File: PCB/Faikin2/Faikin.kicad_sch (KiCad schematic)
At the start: 30 parts, among them J1 1x5, J2 Prog, Q1 BSS138PS, U1 ESP32-PICO-MINI-02, U2 Barcode, U3 MD8942

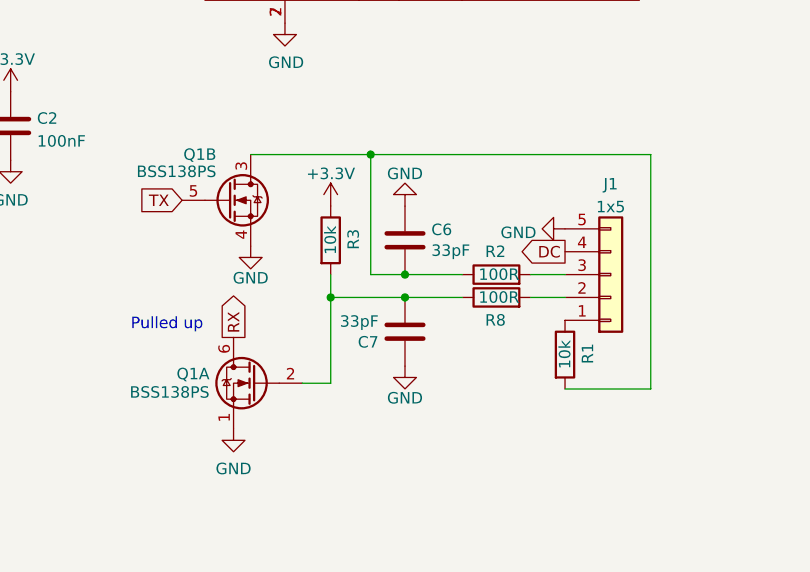
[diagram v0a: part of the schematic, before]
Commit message: New single sided board design
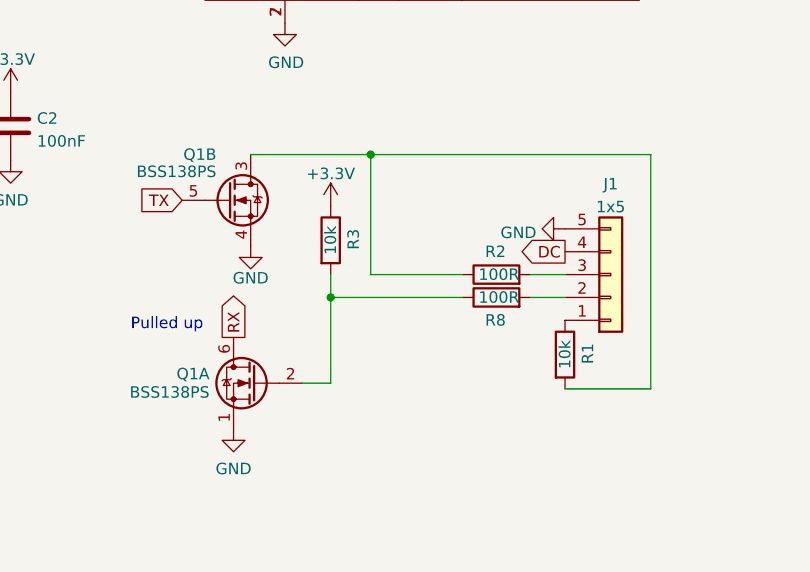
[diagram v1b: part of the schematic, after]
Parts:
- removed C6, C7: 33pF, RevK:C_0402, symbol Device:C
- Q1: LCSC Part # C193381 -> C2912548
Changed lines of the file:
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@@
     (comment 2 "www.me.uk")
   )
-  (junction (at 143.51 88.9) (diameter 0) (color 0 0 0 0)
-  )
   (junction (at 50.8 43.18) (diameter 0) (color 0 0 0 0)
   )
   (junction (at 50.8 27.94) (diameter 0) (color 0 0 0 0)
-  )
-  (junction (at 143.51 91.44) (diameter 0) (color 0 0 0 0)
   )
   (junction (at 81.28 52.07) (diameter 0) (color 0 0 0 0)
@@
     (stroke (width 0) (type default))
   )
-  (wire (pts (xy 143.51 91.44) (xy 149.86 91.44))
+  (wire (pts (xy 135.255 91.44) (xy 149.86 91.44))
     (stroke (width 0) (type default))
   )
@@
     (stroke (width 0) (type default))
   )
-  (wire (pts (xy 139.7 88.9) (xy 143.51 88.9))
-    (stroke (width 0) (type default))
-  )
   (wire (pts (xy 170.815 75.565) (xy 170.815 101.6))
     (stroke (width 0) (type default))
@@
     (stroke (width 0) (type default))
   )
-  (wire (pts (xy 135.255 91.44) (xy 143.51 91.44))
-    (stroke (width 0) (type default))
-  )
   (wire (pts (xy 81.28 52.07) (xy 86.36 52.07))
     (stroke (width 0) (type default))
@@
     (stroke (width 0) (type default))
   )
-  (wire (pts (xy 143.51 88.9) (xy 149.86 88.9))
+  (wire (pts (xy 139.7 88.9) (xy 149.86 88.9))
     (stroke (width 0) (type default))
   )
@@
     )
   )
-  (symbol (lib_id "Device:C") (at 143.51 95.25 180) (unit 1)
-    (in_bom yes) (on_board yes) (dnp no)
-    (property "Reference" "C7" (at 140.589 96.4184 0)
-      (effects (font (size 1.27 1.27)) (justify left))
-    )
-    (property "Value" "33pF" (at 140.589 94.107 0)
-      (effects (font (size 1.27 1.27)) (justify left))
-    )
-    (property "Footprint" "RevK:C_0402" (at 142.5448 91.44 0)
-      (effects (font (size 1.27 1.27)) hide)
-    )
-    (property "Datasheet" "" (at 143.51 95.25 0)
-      (effects (font (size 1.27 1.27)) hide)
-    )
-    (property "Note" "" (at 143.51 95.25 0)
-      (effects (font (size 1.27 1.27)) hide)
-    )
-    (property "Manufacturer" "" (at 143.51 95.25 0)
-      (effects (font (size 1.27 1.27)) hide)
-    )
-    (pin "1")
-    (pin "2")
-    (instances
-      (project "Faikin"
-        (path "/46c350bb-7de4-4e81-aafd-4af55e37aab0"
-          (reference "C7") (unit 1)
-        )
-      )
-    )
-  )
   (symbol (lib_id "Device:C") (at 99.695 72.39 0) (unit 1)
     (in_bom yes) (on_board yes) (dnp no) (fields_autoplaced)
@@
       (effects (font (size 1.27 1.27)) hide)
     )
-    (property "LCSC Part #" "C193381" (at 133.35 74.676 0)
+    (property "LCSC Part #" "C2912548" (at 133.35 74.676 0)
       (effects (font (size 1.27 1.27)) hide)
     )
@@
     )
   )
-  (symbol (lib_id "Device:C") (at 143.51 85.09 0) (unit 1)
-    (in_bom yes) (on_board yes) (dnp no)
-    (property "Reference" "C6" (at 146.431 83.9216 0)
-      (effects (font (size 1.27 1.27)) (justify left))
-    )
-    (property "Value" "33pF" (at 146.431 86.233 0)
-      (effects (font (size 1.27 1.27)) (justify left))
-    )
-    (property "Footprint" "RevK:C_0402" (at 144.4752 88.9 0)
-      (effects (font (size 1.27 1.27)) hide)
-    )
-    (property "Datasheet" "" (at 143.51 85.09 0)
-      (effects (font (size 1.27 1.27)) hide)
-    )
-    (property "Note" "" (at 143.51 85.09 0)
-      (effects (font (size 1.27 1.27)) hide)
-    )
-    (property "Manufacturer" "" (at 143.51 85.09 0)
-      (effects (font (size 1.27 1.27)) hide)
-    )
-    (pin "1")
-    (pin "2")
-    (instances
-      (project "Faikin"
-        (path "/46c350bb-7de4-4e81-aafd-4af55e37aab0"
-          (reference "C6") (unit 1)
-        )
-      )
-    )
-  )
   (symbol (lib_id "Device:R") (at 153.67 88.9 90) (unit 1)
     (in_bom yes) (on_board yes) (dnp no)
@@
         (path "/babeabf2-f3b0-4ed5-8d9e-0215947e6cf3"
           (reference "R8") (unit 1)
-        )
-      )
-    )
-  )
-  (symbol (lib_id "power:GND") (at 143.51 99.06 0) (unit 1)
-    (in_bom yes) (on_board yes) (dnp no) (fields_autoplaced)
-    (property "Reference" "#PWR0112" (at 143.51 105.41 0)
-      (effects (font (size 1.27 1.27)) hide)
-    )
-    (property "Value" "GND" (at 143.51 102.6358 0)
-      (effects (font (size 1.27 1.27)))
-    )
-    (property "Footprint" "" (at 143.51 99.06 0)
-      (effects (font (size 1.27 1.27)) hide)
-    )
-    (property "Datasheet" "" (at 143.51 99.06 0)
-      (effects (font (size 1.27 1.27)) hide)
-    )
-    (pin "1")
-    (instances
-      (project "Faikin"
-        (path "/46c350bb-7de4-4e81-aafd-4af55e37aab0"
-          (reference "#PWR0112") (unit 1)
         )
       )
@@
       (effects (font (size 1.27 1.27)) hide)
     )
-    (property "LCSC Part #" "C193381" (at 117.475 94.996 0)
+    (property "LCSC Part #" "C2912548" (at 117.475 94.996 0)
       (effects (font (size 1.27 1.27)) hide)
     )
@@
         )
       )
-    )
-  )
-  (symbol (lib_id "power:GND") (at 143.51 81.28 180) (unit 1)
-    (in_bom yes) (on_board yes) (dnp no) (fields_autoplaced)
-    (property "Reference" "#PWR0111" (at 143.51 74.93 0)
-      (effects (font (size 1.27 1.27)) hide)
-    )
-    (property "Value" "GND" (at 143.51 77.7042 0)
-      (effects (font (size 1.27 1.27)))
-    )
-    (property "Footprint" "" (at 143.51 81.28 0)
-      (effects (font (size 1.27 1.27)) hide)
-    )
-    (property "Datasheet" "" (at 143.51 81.28 0)
-      (effects (font (size 1.27 1.27)) hide)
-    )
-    (pin "1")
-    (instances
-      (project "Faikin"
-        (path "/46c350bb-7de4-4e81-aafd-4af55e37aab0"
-          (reference "#PWR0111") (unit 1)
-        )
-      )

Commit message: As ordered
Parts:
- added C3, C4: 33pF, RevK:C_0402, symbol Device:C
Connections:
- net GND: now also C3.1, C4.1
- net at Q1.2 (GN), R3.2, R8.1: now also C4.2
- net at Q1.3 (SP), R1.2, R2.1: now also C3.2
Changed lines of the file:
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@@
   (junction (at 81.28 57.15) (diameter 0) (color 0 0 0 0)
+  )
+  (junction (at 143.51 91.44) (diameter 0) (color 0 0 0 0)
+  )
+  (junction (at 143.51 88.9) (diameter 0) (color 0 0 0 0)
   )
   (no_connect (at 81.28 71.12))
@@
     (stroke (width 0) (type default))
   )
-  (wire (pts (xy 135.255 91.44) (xy 149.86 91.44))
+  (wire (pts (xy 135.255 91.44) (xy 143.51 91.44))
     (stroke (width 0) (type default))
   )
@@
     (stroke (width 0) (type default))
   )
+  (wire (pts (xy 143.51 88.9) (xy 149.86 88.9))
+    (stroke (width 0) (type default))
+  )
   (wire (pts (xy 170.815 75.565) (xy 170.815 101.6))
     (stroke (width 0) (type default))
@@
     (stroke (width 0) (type default))
   )
-  (wire (pts (xy 139.7 88.9) (xy 149.86 88.9))
+  (wire (pts (xy 139.7 88.9) (xy 143.51 88.9))
     (stroke (width 0) (type default))
   )
   (wire (pts (xy 139.7 75.565) (xy 139.7 88.9))
+    (stroke (width 0) (type default))
+  )
+  (wire (pts (xy 143.51 91.44) (xy 149.86 91.44))
     (stroke (width 0) (type default))
   )
@@
     )
   )
+  (symbol (lib_id "power:GND") (at 143.51 99.06 0) (unit 1)
+    (in_bom yes) (on_board yes) (dnp no) (fields_autoplaced)
+    (property "Reference" "#PWR010" (at 143.51 105.41 0)
+      (effects (font (size 1.27 1.27)) hide)
+    )
+    (property "Value" "GND" (at 143.51 102.6358 0)
+      (effects (font (size 1.27 1.27)))
+    )
+    (property "Footprint" "" (at 143.51 99.06 0)
+      (effects (font (size 1.27 1.27)) hide)
+    )
+    (property "Datasheet" "" (at 143.51 99.06 0)
+      (effects (font (size 1.27 1.27)) hide)
+    )
+    (pin "1")
+    (instances
+      (project "Faikin"
+        (path "/46c350bb-7de4-4e81-aafd-4af55e37aab0"
+          (reference "#PWR010") (unit 1)
+        )
+      )
+    )
+  )
   (symbol (lib_id "Device:R") (at 64.77 27.94 270) (unit 1)
     (in_bom yes) (on_board yes) (dnp no)
@@
         (path "/46c350bb-7de4-4e81-aafd-4af55e37aab0"
           (reference "PCB1") (unit 1)
+        )
+      )
+    )
+  )
+  (symbol (lib_id "power:GND") (at 143.51 81.28 180) (unit 1)
+    (in_bom yes) (on_board yes) (dnp no) (fields_autoplaced)
+    (property "Reference" "#PWR07" (at 143.51 74.93 0)
+      (effects (font (size 1.27 1.27)) hide)
+    )
+    (property "Value" "GND" (at 143.51 77.7042 0)
+      (effects (font (size 1.27 1.27)))
+    )
+    (property "Footprint" "" (at 143.51 81.28 0)
+      (effects (font (size 1.27 1.27)) hide)
+    )
+    (property "Datasheet" "" (at 143.51 81.28 0)
+      (effects (font (size 1.27 1.27)) hide)
+    )
+    (pin "1")
+    (instances
+      (project "Faikin"
+        (path "/46c350bb-7de4-4e81-aafd-4af55e37aab0"
+          (reference "#PWR07") (unit 1)
         )
       )
@@
     )
   )
+  (symbol (lib_id "Device:C") (at 143.51 95.25 180) (unit 1)
+    (in_bom yes) (on_board yes) (dnp no)
+    (property "Reference" "C4" (at 140.589 96.4184 0)
+      (effects (font (size 1.27 1.27)) (justify left))
+    )
+    (property "Value" "33pF" (at 140.589 94.107 0)
+      (effects (font (size 1.27 1.27)) (justify left))
+    )
+    (property "Footprint" "RevK:C_0402" (at 142.5448 91.44 0)
+      (effects (font (size 1.27 1.27)) hide)
+    )
+    (property "Datasheet" "" (at 143.51 95.25 0)
+      (effects (font (size 1.27 1.27)) hide)
+    )
+    (property "Note" "" (at 143.51 95.25 0)
+      (effects (font (size 1.27 1.27)) hide)
+    )
+    (property "Manufacturer" "" (at 143.51 95.25 0)
+      (effects (font (size 1.27 1.27)) hide)
+    )
+    (pin "1")
+    (pin "2")
+    (instances
+      (project "Faikin"
+        (path "/46c350bb-7de4-4e81-aafd-4af55e37aab0"
+          (reference "C4") (unit 1)
+        )
+      )
+    )
+  )
   (symbol (lib_id "RevK:Hidden") (at 151.13 46.99 0) (unit 1)
     (in_bom yes) (on_board yes) (dnp no)
@@
         )
       )
+    )
+  )
+  (symbol (lib_id "Device:C") (at 143.51 85.09 0) (unit 1)
+    (in_bom yes) (on_board yes) (dnp no)
+    (property "Reference" "C3" (at 146.431 83.9216 0)
+      (effects (font (size 1.27 1.27)) (justify left))
+    )
+    (property "Value" "33pF" (at 146.431 86.233 0)
+      (effects (font (size 1.27 1.27)) (justify left))
+    )
+    (property "Footprint" "RevK:C_0402" (at 144.4752 88.9 0)
+      (effects (font (size 1.27 1.27)) hide)
+    )
+    (property "Datasheet" "" (at 143.51 85.09 0)
+      (effects (font (size 1.27 1.27)) hide)
+    )
+    (property "Note" "" (at 143.51 85.09 0)
+      (effects (font (size 1.27 1.27)) hide)
+    )
+    (property "Manufacturer" "" (at 143.51 85.09 0)
+      (effects (font (size 1.27 1.27)) hide)
+    )
+    (pin "1")
+    (pin "2")
+    (instances
+      (project "Faikin"
+        (path "/46c350bb-7de4-4e81-aafd-4af55e37aab0"
+          (reference "C3") (unit 1)
+        )
+      )

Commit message: Silk
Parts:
- added Logo1: AJK, RevK:AJK, symbol RevK:AJK
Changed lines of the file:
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@@
+    )
+  )
+  (symbol (lib_id "RevK:AJK") (at 250.19 174.625 0) (unit 1)
+    (in_bom no) (on_board yes) (dnp no) (fields_autoplaced)
+    (property "Reference" "Logo1" (at 250.19 172.085 0)
+      (effects (font (size 1.27 1.27)) hide)
+    )
+    (property "Value" "AJK" (at 250.825 174.625 0)
+      (effects (font (size 1.27 1.27)) (justify left))
+    )
+    (property "Footprint" "RevK:AJK" (at 250.19 177.165 0)
+      (effects (font (size 1.27 1.27)) hide)
+    )
+    (property "Datasheet" "" (at 250.19 177.165 0)
+      (effects (font (size 1.27 1.27)) hide)
+    )
+    (property "Note" "Non part, PCB printed" (at 250.19 174.625 0)
+      (effects (font (size 1.27 1.27)) hide)
+    )
+    (instances
+      (project "Faikin"
+        (path "/46c350bb-7de4-4e81-aafd-4af55e37aab0"
+          (reference "Logo1") (unit 1)
+        )
+      )
     )
   )

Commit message: Library update
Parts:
- removed R3: 10k, RevK:R_0402, symbol Device:R
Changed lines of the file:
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@@
   (junction (at 81.28 52.07) (diameter 0) (color 0 0 0 0)
-  )
-  (junction (at 135.255 91.44) (diameter 0) (color 0 0 0 0)
   )
   (junction (at 139.7 75.565) (diameter 0) (color 0 0 0 0)
@@
     (stroke (width 0) (type default))
   )
-  (wire (pts (xy 135.255 88.9) (xy 135.255 91.44))
-    (stroke (width 0) (type default))
-  )
   (wire (pts (xy 81.28 52.07) (xy 86.36 52.07))
     (stroke (width 0) (type default))
@@
         )
       )
-    )
-  )
-  (symbol (lib_id "Device:R") (at 135.255 85.09 0) (unit 1)
-    (in_bom yes) (on_board yes) (dnp no)
-    (property "Reference" "R3" (at 137.795 83.82 90)
-      (effects (font (size 1.27 1.27)) (justify right))
-    )
-    (property "Value" "10k" (at 135.255 85.09 90)
-      (effects (font (size 1.27 1.27)))
-    )
-    (property "Footprint" "RevK:R_0402" (at 133.477 85.09 90)
-      (effects (font (size 1.27 1.27)) hide)
-    )
-    (property "Datasheet" "~" (at 135.255 85.09 0)
-      (effects (font (size 1.27 1.27)) hide)
-    )
-    (pin "1")
-    (pin "2")
-    (instances
-      (project "Faikin"
-        (path "/46c350bb-7de4-4e81-aafd-4af55e37aab0"
-          (reference "R3") (unit 1)
-        )
-      )
-    )
-  )
-  (symbol (lib_id "power:+3.3V") (at 135.255 81.28 0) (unit 1)
-    (in_bom yes) (on_board yes) (dnp no) (fields_autoplaced)
-    (property "Reference" "#PWR06" (at 135.255 85.09 0)
-      (effects (font (size 1.27 1.27)) hide)
-    )
-    (property "Value" "+3.3V" (at 135.255 77.7042 0)
-      (effects (font (size 1.27 1.27)))
-    )
-    (property "Footprint" "" (at 135.255 81.28 0)
-      (effects (font (size 1.27 1.27)) hide)
-    )
-    (property "Datasheet" "" (at 135.255 81.28 0)
-      (effects (font (size 1.27 1.27)) hide)
-    )
-    (pin "1")
-    (instances
-      (project "Faikin"
-        (path "/46c350bb-7de4-4e81-aafd-4af55e37aab0"
-          (reference "#PWR06") (unit 1)
-        )
-      )

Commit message: Mainly #83
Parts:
- J1: LCSC Part # C225427 -> C265103
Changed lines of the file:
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@@
       (effects (font (size 1.27 1.27)) hide)
     )
-    (property "LCSC Part #" "C225427" (at 166.37 88.9 0)
+    (property "LCSC Part #" "C265103" (at 166.37 88.9 0)
       (effects (font (size 1.27 1.27)) hide)
     )

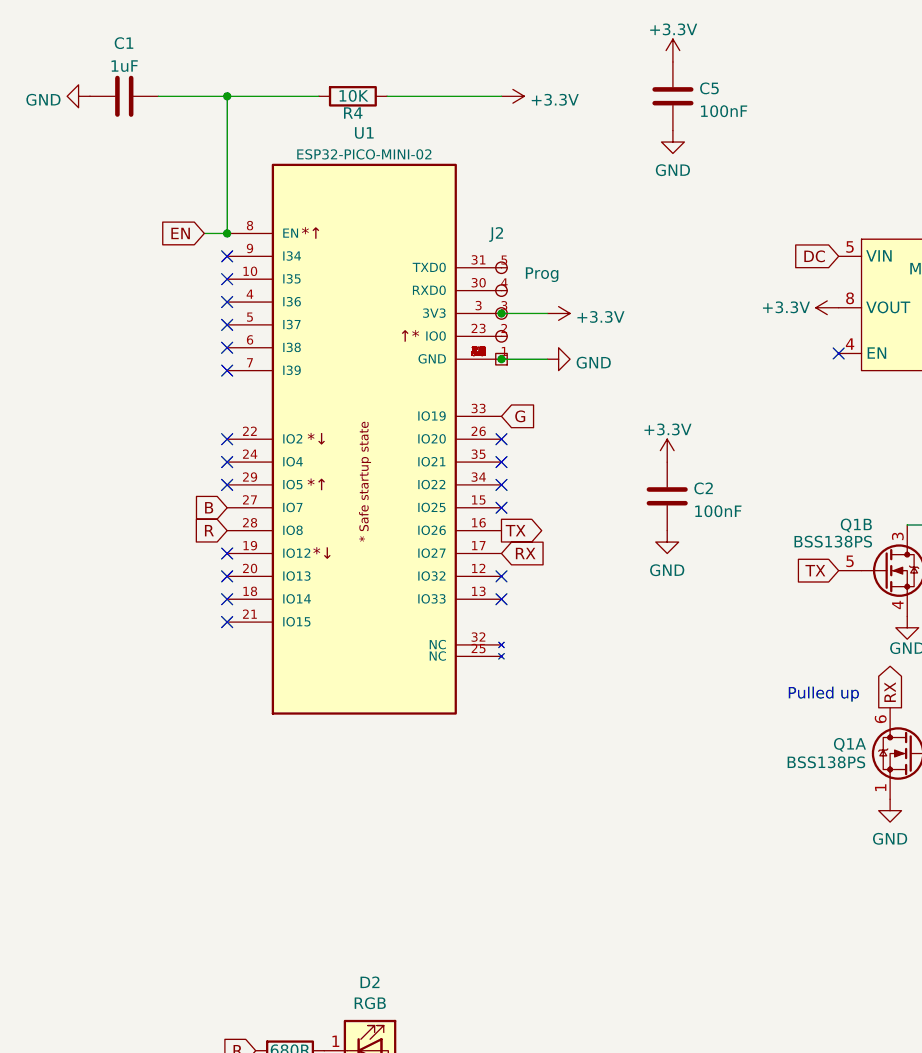
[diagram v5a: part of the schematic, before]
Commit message: Faikin2 confirmed working, now replaces Faikin 1
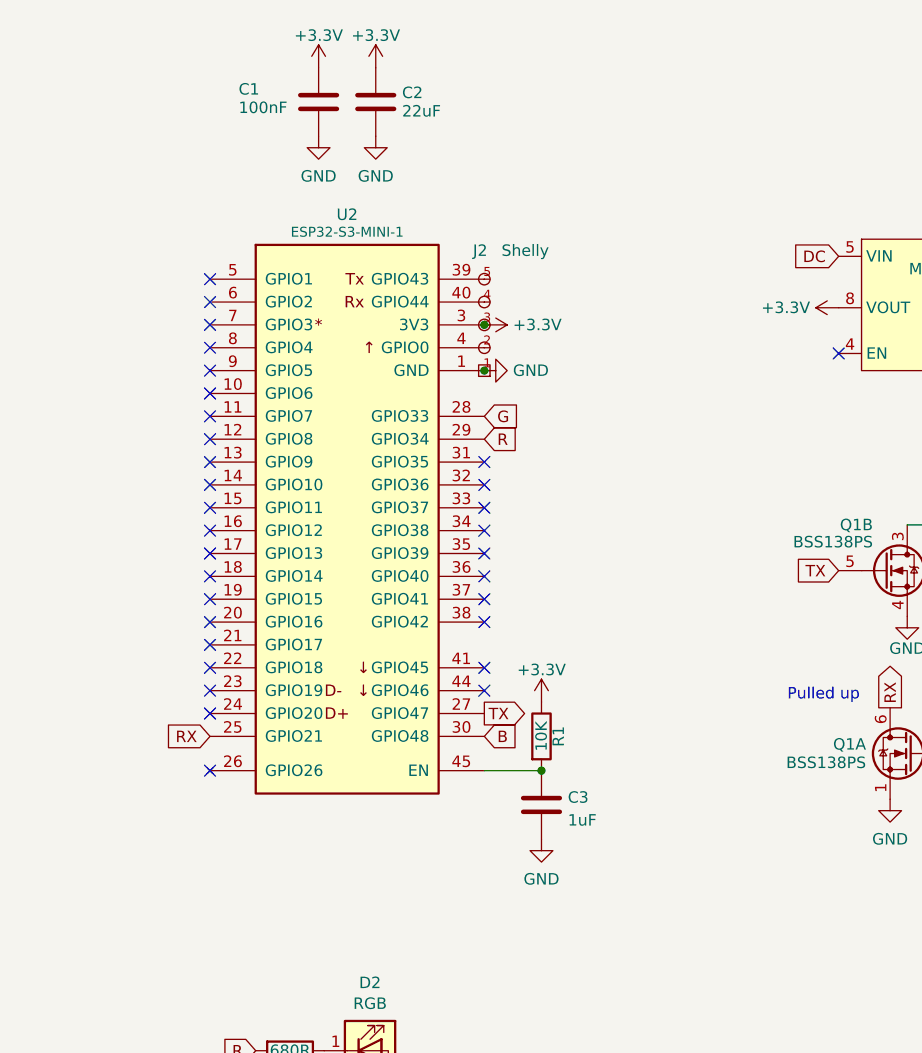
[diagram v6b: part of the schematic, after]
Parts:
- removed C5: 100nF, RevK:C_0402, symbol Device:C
- removed R4: 10K, RevK:R_0402, symbol Device:R
- removed U1: ESP32-PICO-MINI-02, RevK:ESP32-PICO-MINI-02, symbol RevK:ESP32-PICO-MINI-02
- added C3: 1uF, RevK:C_0402, symbol Device:C
- added R1: 10K, RevK:R_0402, symbol Device:R
- added U2: ESP32-S3-MINI-1, RevK:ESP32-S3-MINI-1, symbol RevK:ESP32-S3-MINI-1-N4R2
- C1: value 1uF -> 100nF
- C2: value 100nF -> 22uF
- J2: value Prog -> Shelly
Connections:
- net EN is gone; now on net GND: C1.2
- net +3.3V: now also C1.1, R1.1, U2.3 (3V3)
- net B: now also U2.30 (GPIO48)
- net G: now also U2.28 (GPIO33)
- net GND: now also C3.2, U2.1 (GND), U2.2 (GND), U2.42 (GND), U2.43 (GND), U2.46 (GND), U2.47 (GND), U2.48 (GND), U2.49 (GND), U2.50 (GND), U2.51 (GND), U2.52 (GND), U2.53 (GND), U2.54 (GND), U2.55 (GND), U2.56 (GND), U2.57 (GND), U2.58 (GND), U2.59 (GND), U2.60 (GND), U2.61 (GND), U2.62 (GND), U2.63 (GND), U2.64 (GND), U2.65 (GND); no longer C1.1
- net R: now also U2.29 (GPIO34)
- net RX: now also U2.25 (GPIO21)
- net TX: now also U2.27 (GPIO47)
- net at J2.2 (0): now also U2.4 (GPIO0)
- net at J2.4 (Rx): now also U2.40 (GPIO44)
- net at J2.5 (Tx): now also U2.39 (GPIO43)
- new net: C3.1, R1.2, U2.45 (EN)
- no-connect marks 20 -> 32
